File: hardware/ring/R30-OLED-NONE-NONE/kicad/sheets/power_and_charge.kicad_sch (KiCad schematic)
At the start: 0 parts

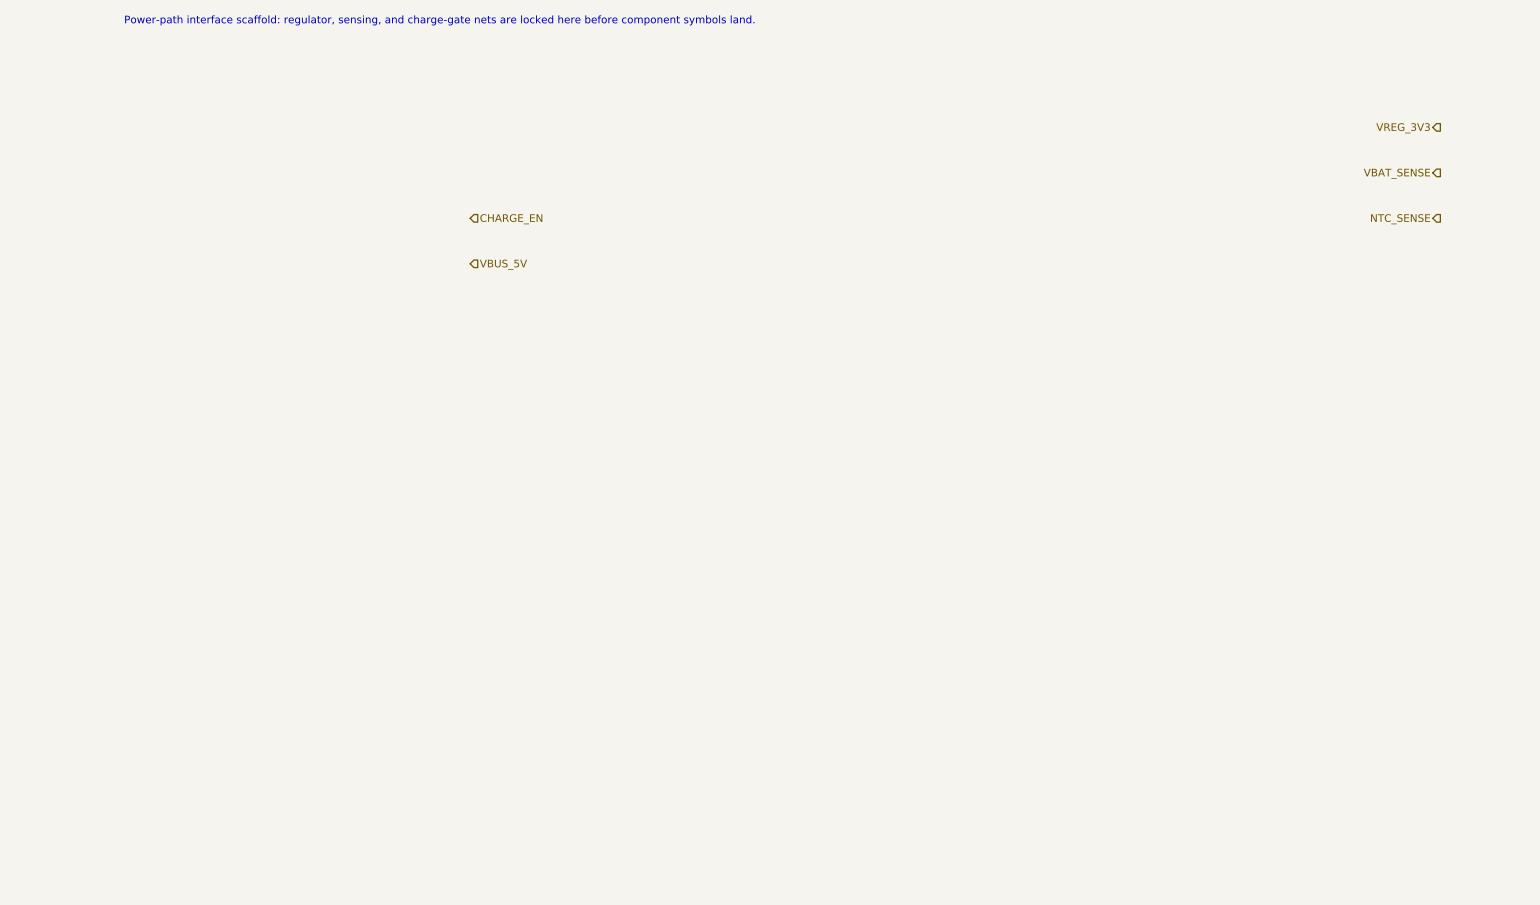
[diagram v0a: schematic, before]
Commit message: trial(mcp-sch): populate R30 power_and_charge sub-sheet via kicad-sch-api
Adds 17 charge-path BOM components (U3, U4, Q1, Q2, R1, R3, R4, R6, R7,
R8, R9, R10, R11, NTC1, C1, C2, C3) to the power_and_charge sub-sheet
using stock KiCad symbols + footprints. The lib_symbols block aggregates
correctly (the specific defect that disqualified kicad-mcp-pro v3.1.3
in the prior trial). All 5 existing hierarchical labels preserved
verbatim with original UUIDs.

Trial-only commit. Do not merge until BDFL review per the trial brief.

Co-Authored-By: Claude Opus 4.7 (1M context) <noreply@anthropic.com>
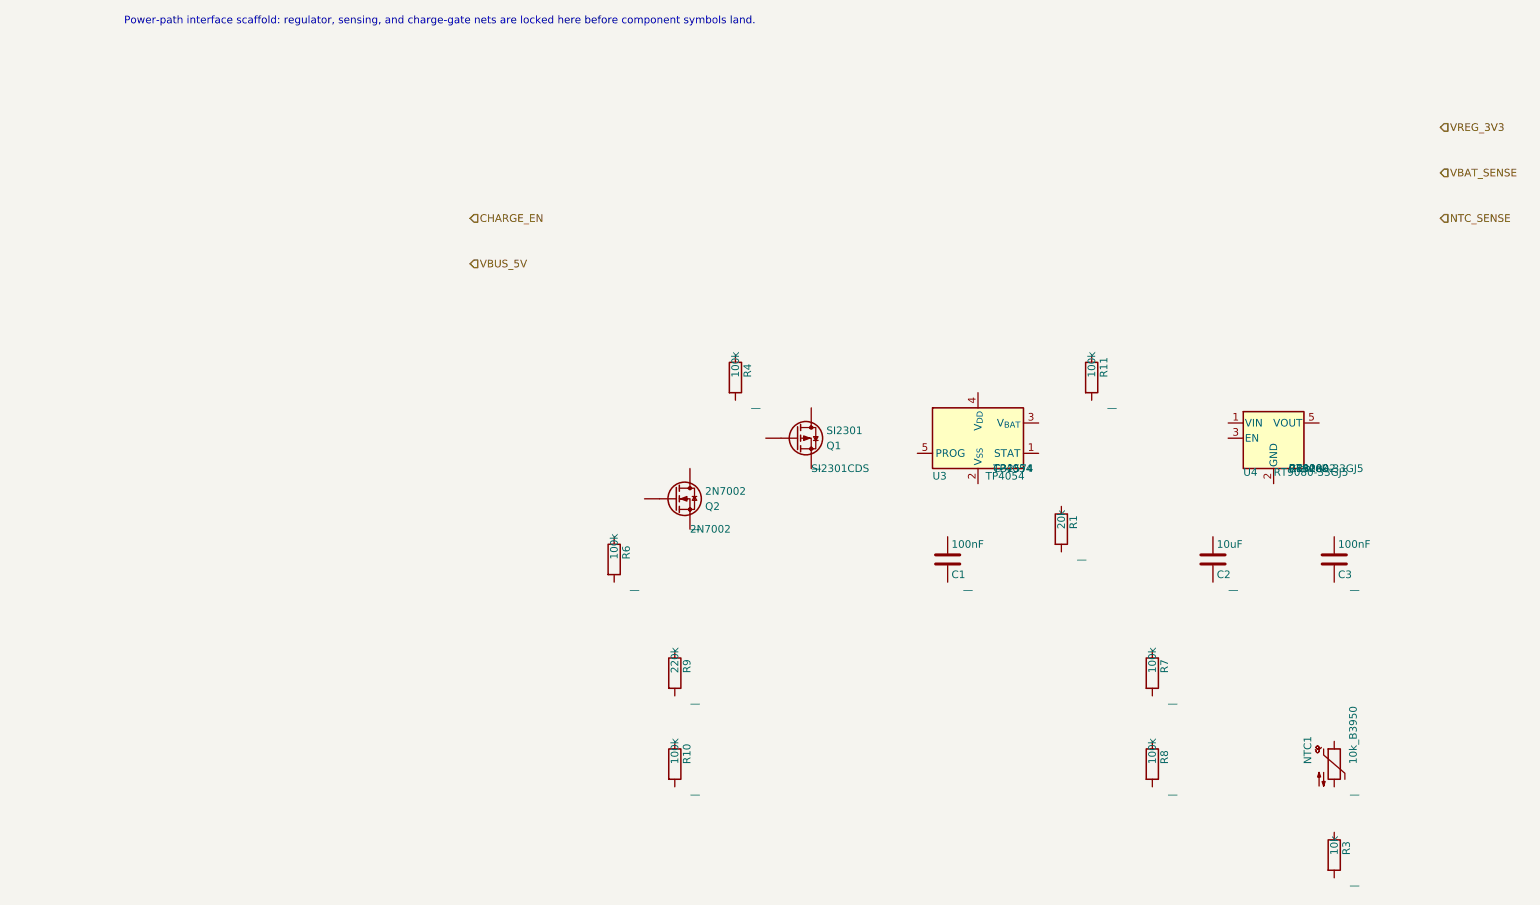
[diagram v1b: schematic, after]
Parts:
- added C1, C3: 100nF, Capacitor_SMD:C_0402_1005Metric, symbol Device:C
- added C2: 10uF, Capacitor_SMD:C_0402_1005Metric, symbol Device:C
- added NTC1: 10k_B3950, Resistor_SMD:R_0402_1005Metric, symbol Device:Thermistor_NTC
- added Q1: SI2301, Package_TO_SOT_SMD:SOT-23, symbol Device:Q_PMOS
- added Q2: 2N7002, Package_TO_SOT_SMD:SOT-23, symbol Device:Q_NMOS
- added R1: 20k, Resistor_SMD:R_0402_1005Metric, symbol Device:R
- added R10, R11, R4, R6, R7, R8: 100k, Resistor_SMD:R_0402_1005Metric, symbol Device:R
- added R3: 10k, Resistor_SMD:R_0402_1005Metric, symbol Device:R
- added R9: 220k, Resistor_SMD:R_0402_1005Metric, symbol Device:R
- added U3: TP4054, Package_TO_SOT_SMD:SOT-23-5, symbol Battery_Management:MCP73831-2-OT
- added U4: RT9080-33GJ5, Package_TO_SOT_SMD:SOT-23-5, symbol Regulator_Linear:AP2112K-3.3

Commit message: trial(mcp-sch): wire R30 power_and_charge with net labels and power flags
Adds 41 wire labels (one per pin) declaring the charge-path topology:
VBUS_5V, VBUS_CHG, Q1_GATE, VBAT_PROTECTED, VREG_3V3, GND, NTC_SENSE,
VBAT_SENSE, CHARGE_EN, CHRG_STAT_INT, U3_PROG, VBUS_DETECT_INT.

Adds 4 power symbols to silence power_pin_not_driven warnings on U3:
- 2× PWR_FLAG on VBUS_5V and VBUS_CHG (declare external power source
  and post-MOSFET rail as driven)
- 1× power:GND + 1× PWR_FLAG on GND (joined by a wire) so GND has a
  power-output reference

Result: /power_and_charge/ sub-sheet drops from 41 violations (post-
populate) to 0. Remaining 72 violations are on the root sheet (pre-
existing label_dangling/endpoint_off_grid) or environmental (no
project sym-lib-table or fp-lib-table — addressed in PREREQ 3).

Note: ksa.components.add does not auto-propagate the lib_symbol's
default Value property when none is passed. Power symbols therefore
need their net name passed explicitly as `value=` (otherwise the
instance has empty Value, which KiCad ERC reports as a
multiple_net_names conflict).

Co-Authored-By: Claude Opus 4.7 (1M context) <noreply@anthropic.com>
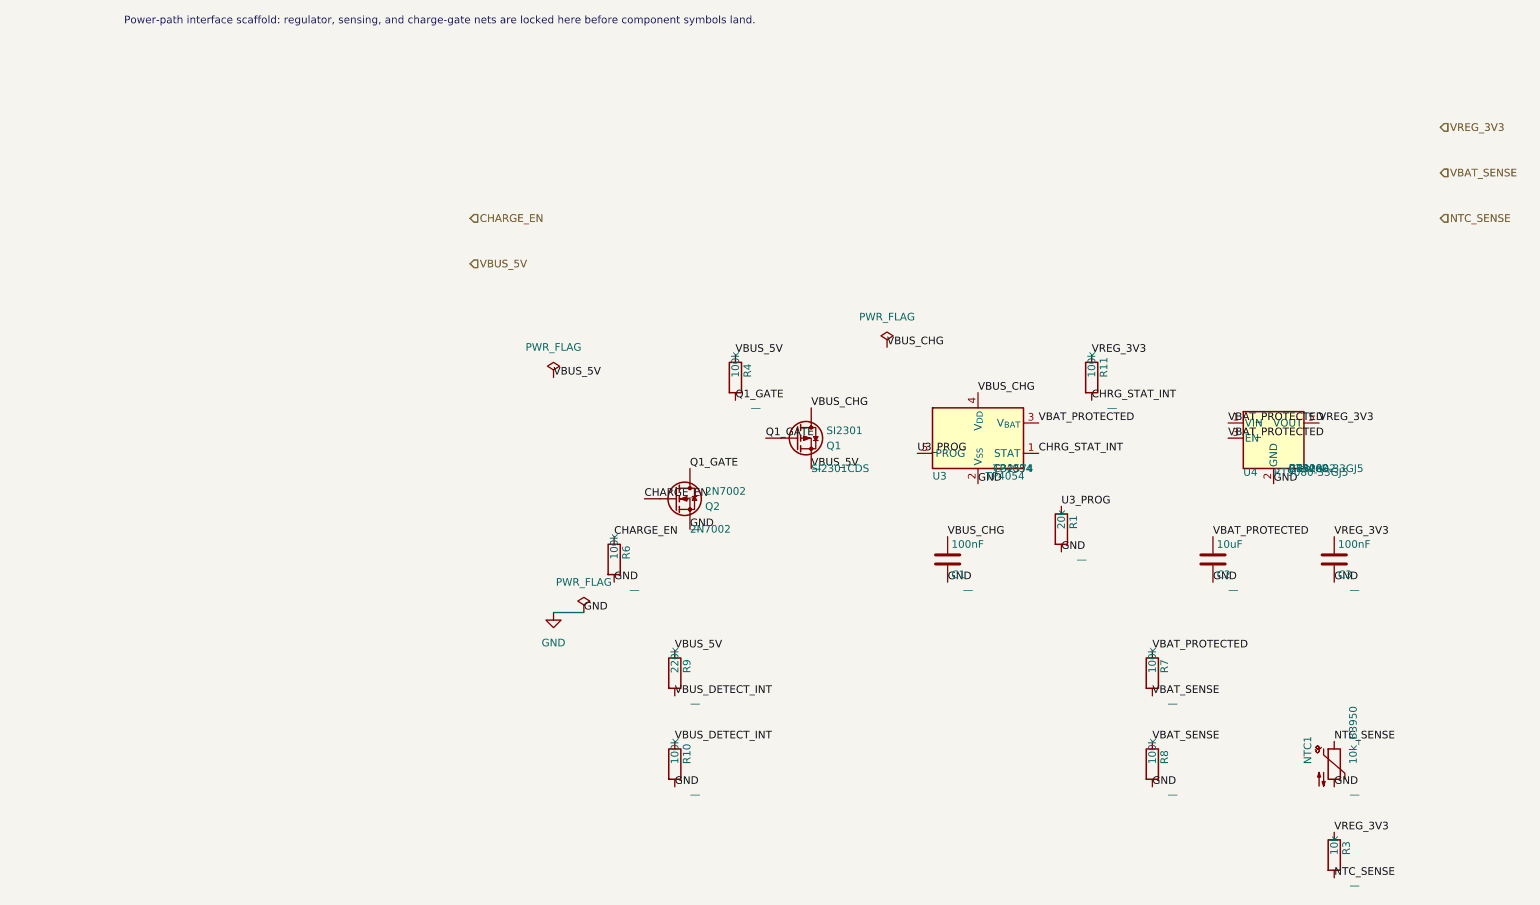
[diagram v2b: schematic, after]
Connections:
- net CHARGE_EN: now also Q2.G, R6.1
- net NTC_SENSE: now also NTC1.1, R3.2
- net VBAT_SENSE: now also R7.2, R8.1
- net VBUS_5V: now also Q1.S, R4.1, R9.1
- net VREG_3V3: now also C3.1, R11.1, R3.1, U4.5 (VOUT)
- net CHRG_STAT_INT: now reaches U3.1 (STAT)
- net CHRG_STAT_INT: now also R11.2
- net GND: now reaches U3.2 (V_{SS})
- net GND: now also C1.2, C2.2, C3.2, NTC1.2, Q2.S, R1.2, R10.2, R6.2, R8.2, U4.2 (GND)
- net VBAT_PROTECTED: now reaches U3.3 (V_{BAT})
- net VBAT_PROTECTED: now also C2.1, R7.1, U4.1 (VIN), U4.3 (EN)
- net VBUS_CHG: now reaches U3.4 (V_{DD})
- net VBUS_CHG: now also C1.1, Q1.D
- net U3_PROG: now reaches U3.5 (PROG)
- net U3_PROG: now also R1.1
- net Q1_GATE: now reaches R4.2
- net Q1_GATE: now also Q1.G, Q2.D
- net VBUS_DETECT_INT: now reaches R10.1
- net VBUS_DETECT_INT: now also R9.2
